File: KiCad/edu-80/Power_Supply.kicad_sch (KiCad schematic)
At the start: 19 parts, among them P1 Wall plug, Q21 2N3055, Q22 2N3906, SW1 SW_SPST, U22 uA7805

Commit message: Cleaning up the PAL-003 decoding, adding Modifications page.
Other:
- company: (none) -> Strangers
- title: (none) -> Edu-80 Z80 Trainer
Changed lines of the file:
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@@
 (kicad_sch (version 20230121) (generator eeschema)
   (paper "A")
+  (title_block
+    (title "Edu-80 Z80 Trainer")
+    (date "2023-06-03")
+    (rev "0.1")
+    (company "Strangers")
+    (comment 1 "Author: James D. Tucker")
+  )
   (junction (at 193.04 77.47) (diameter 0) (color 0 0 0 0)
   )

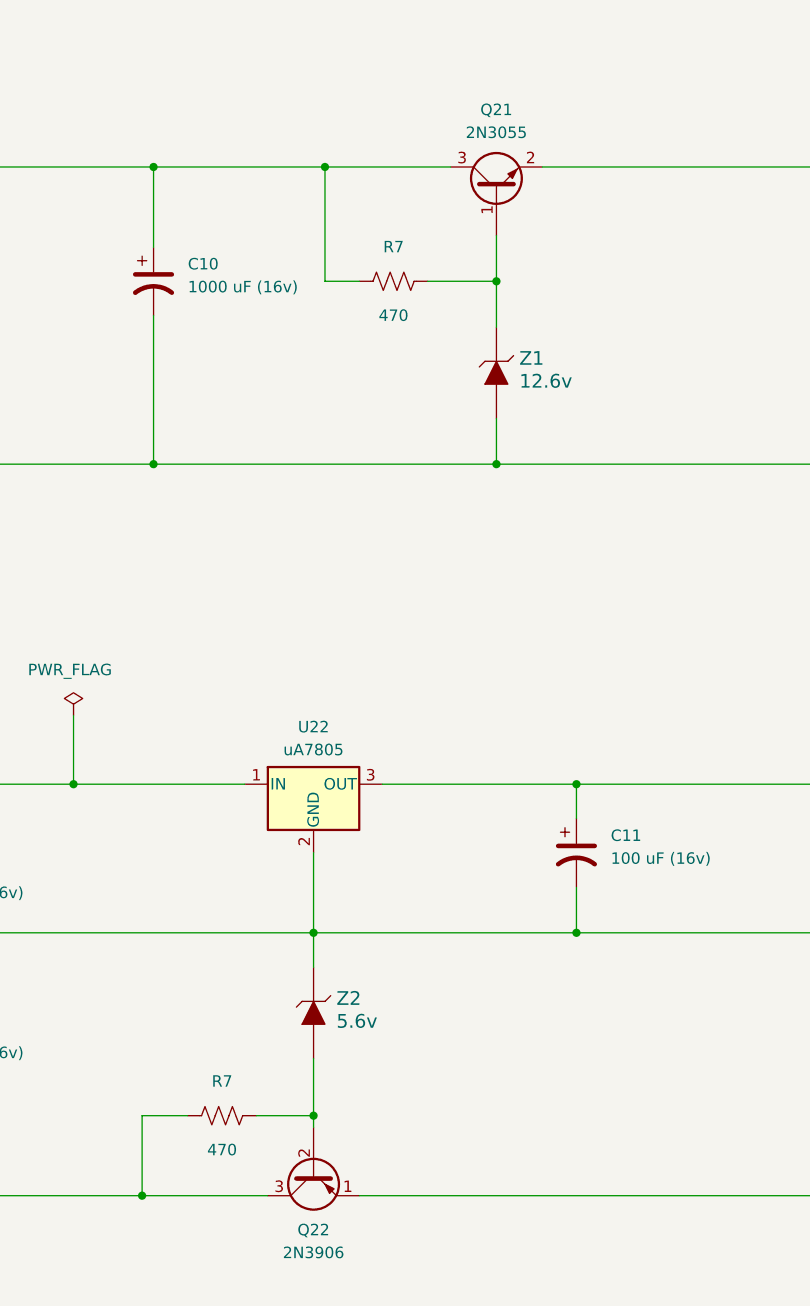
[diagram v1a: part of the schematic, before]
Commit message: Fixed ~IRQ vs. INT for PIO/CTC. Removed old (version 5) schematic files.
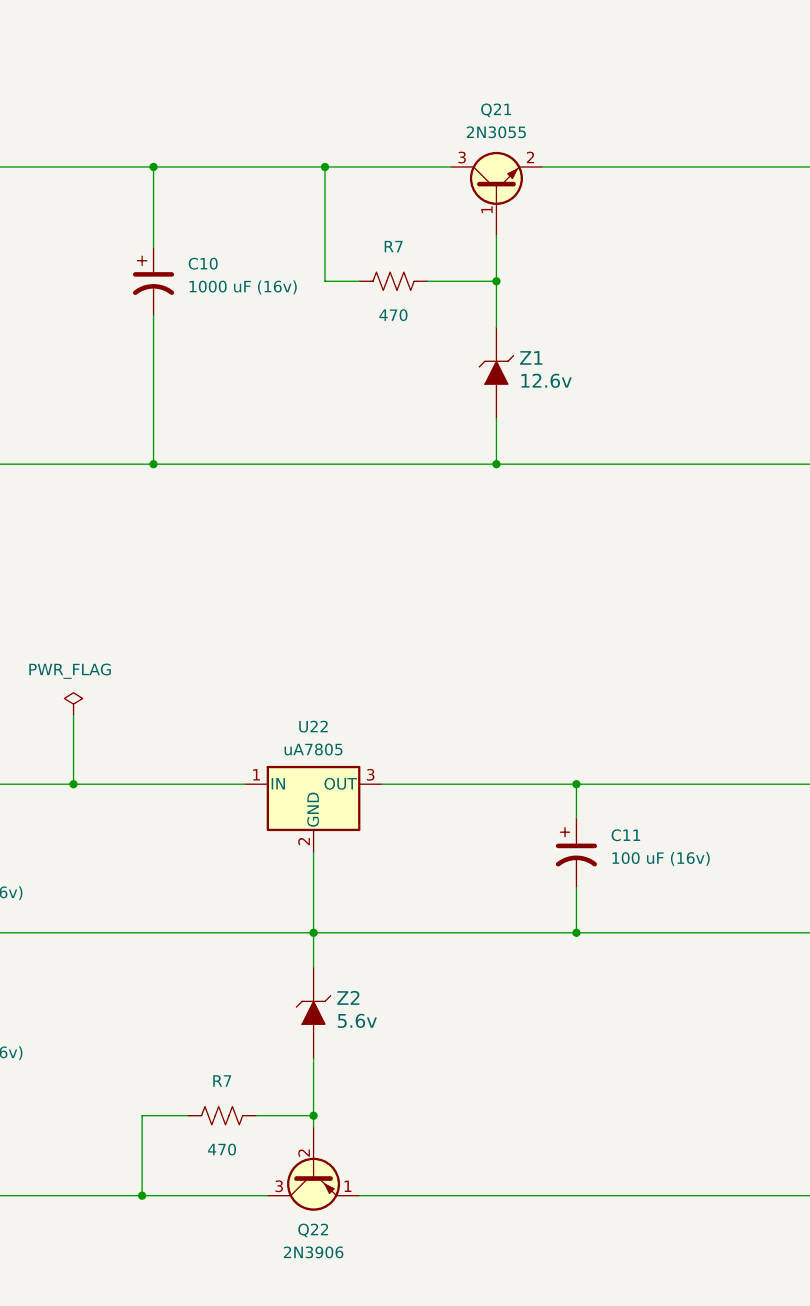
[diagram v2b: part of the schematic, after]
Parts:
- Q21: symbol Transistor_BJT:2N3055 -> Edu-80_Symbols:2N3055
- Q22: symbol Transistor_BJT:2N3906 -> Edu-80_Symbols:2N3905
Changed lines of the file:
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@@
   (title_block
     (title "Edu-80 Z80 Trainer")
-    (date "2023-06-03")
+    (date "2023-06-05")
     (rev "0.1")
     (company "Strangers")
-    (comment 1 "Author: James D. Tucker")
+    (comment 4 "Author: James D. Tucker")
   )
   (junction (at 193.04 77.47) (diameter 0) (color 0 0 0 0)
@@
     )
   )
-  (symbol (lib_id "Transistor_BJT:2N3906") (at 172.72 156.21 90) (mirror x) (unit 1)
+  (symbol (lib_id "Edu-80_Symbols:2N3905") (at 172.72 156.21 90) (mirror x) (unit 1)
     (in_bom yes) (on_board yes) (dnp no) (fields_autoplaced)
     (property "Reference" "Q22" (at 172.72 162.56 90)
@@
       (effects (font (size 1.27 1.27) italic) (justify left) hide)
     )
-    (property "Datasheet" "https://www.onsemi.com/pub/Collateral/2N3906-D.PDF" (at 172.72 156.21 0)
+    (property "Datasheet" "https://www.nteinc.com/specs/original/2N3905_06.pdf" (at 172.72 156.21 0)
       (effects (font (size 1.27 1.27)) (justify left) hide)
     )
@@
     )
   )
-  (symbol (lib_id "Transistor_BJT:2N3055") (at 193.04 46.99 90) (unit 1)
+  (symbol (lib_id "Edu-80_Symbols:2N3055") (at 193.04 46.99 90) (unit 1)
     (in_bom yes) (on_board yes) (dnp no) (fields_autoplaced)
     (property "Reference" "Q21" (at 193.04 38.1 90)

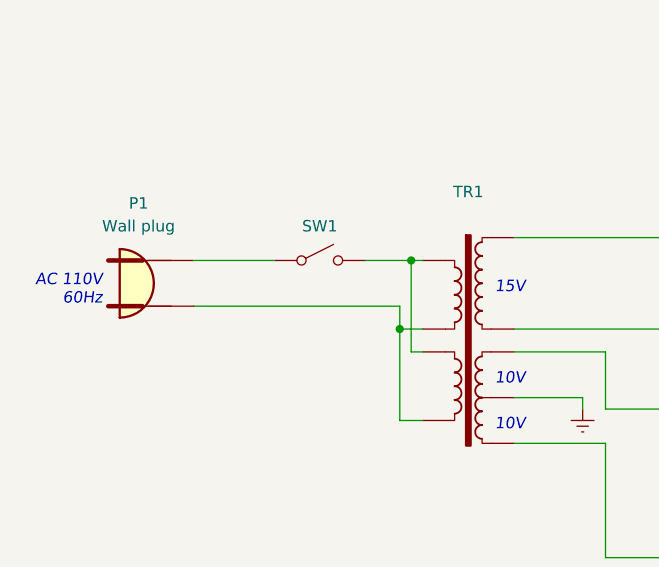
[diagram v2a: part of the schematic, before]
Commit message: Fixed the last of the EDR warnings/errors, adding footprints
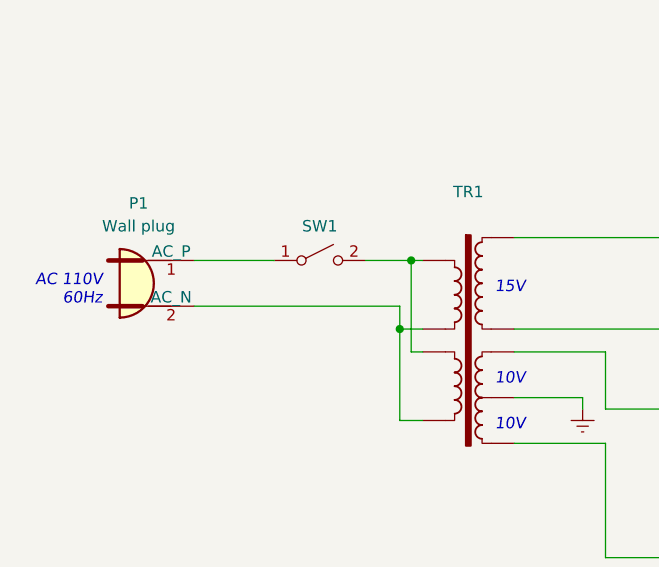
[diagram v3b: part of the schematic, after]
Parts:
- TR1: footprint (none) -> Transformer_THT:Transformer_Breve_TEZ-28x33
- Z1, Z2: footprint (none) -> digikey-footprints:SOD-123; Category (none) -> Discrete Semiconductor Products; Digi-Key_PN (none) -> MMSZ5231B-FDICT-ND; MPN (none) -> MMSZ5231B-7-F
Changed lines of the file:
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@@
       (effects (font (size 1.27 1.27)) hide)
     )
-    (property "Footprint" "" (at 63.5 116.84 0)
+    (property "Footprint" "Transformer_THT:Transformer_Breve_TEZ-28x33" (at 63.5 116.84 0)
       (effects (font (size 1.27 1.27)) hide)
     )
@@
       (effects (font (size 1.524 1.524)) (justify right))
     )
-    (property "Footprint" "" (at 187.96 62.23 0)
-      (effects (font (size 1.524 1.524)) (justify left) hide)
-    )
-    (property "Datasheet" "" (at 185.42 62.23 0)
-      (effects (font (size 1.524 1.524)) (justify left) hide)
-    )
-    (property "Digi-Key_PN" "" (at 182.88 62.23 0)
-      (effects (font (size 1.524 1.524)) (justify left) hide)
-    )
-    (property "MPN" "" (at 180.34 62.23 0)
-      (effects (font (size 1.524 1.524)) (justify left) hide)
-    )
-    (property "Category" "" (at 177.8 62.23 0)
+    (property "Footprint" "digikey-footprints:SOD-123" (at 187.96 62.23 0)
+      (effects (font (size 1.524 1.524)) (justify left) hide)
+    )
+    (property "Datasheet" "https://www.diodes.com/assets/Datasheets/ds18010.pdf" (at 185.42 62.23 0)
+      (effects (font (size 1.524 1.524)) (justify left) hide)
+    )
+    (property "Digi-Key_PN" "MMSZ5231B-FDICT-ND" (at 182.88 62.23 0)
+      (effects (font (size 1.524 1.524)) (justify left) hide)
+    )
+    (property "MPN" "MMSZ5231B-7-F" (at 180.34 62.23 0)
+      (effects (font (size 1.524 1.524)) (justify left) hide)
+    )
+    (property "Category" "Discrete Semiconductor Products" (at 177.8 62.23 0)
       (effects (font (size 1.524 1.524)) (justify left) hide)
     )
@@
       (effects (font (size 1.524 1.524)) (justify right))
     )
-    (property "Footprint" "" (at 167.64 133.35 0)
-      (effects (font (size 1.524 1.524)) (justify left) hide)
-    )
-    (property "Datasheet" "" (at 165.1 133.35 0)
-      (effects (font (size 1.524 1.524)) (justify left) hide)
-    )
-    (property "Digi-Key_PN" "" (at 162.56 133.35 0)
-      (effects (font (size 1.524 1.524)) (justify left) hide)
-    )
-    (property "MPN" "" (at 160.02 133.35 0)
-      (effects (font (size 1.524 1.524)) (justify left) hide)
-    )
-    (property "Category" "" (at 157.48 133.35 0)
-      (effects (font (size 1.524 1.524)) (justify left) hide)
-    )
+    (property "Footprint" "digikey-footprints:SOD-123" (at 167.64 133.35 0)
+      (effects (font (size 1.524 1.524)) (justify left) hide)
+    )
+    (property "Datasheet" "https://www.diodes.com/assets/Datasheets/ds18010.pdf" (at 165.1 133.35 0)
+      (effects (font (size 1.524 1.524)) (justify left) hide)
+    )
+    (property "Digi-Key_PN" "MMSZ5231B-FDICT-ND" (at 162.56 133.35 0)
+      (effects (font (size 1.524 1.524)) (justify left) hide)
+    )
+    (property "MPN" "MMSZ5231B-7-F" (at 160.02 133.35 0)
+      (effects (font (size 1.524 1.524)) (justify left) hide)
+    )
+    (property "Category" "Discrete Semiconductor Products" (at 157.48 133.35 0)
+      (effects (font (size 1.524 1.524)) (justify left) hide)
+    )

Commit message: Adding footprints.
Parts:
- C10, C11, C12, C13: footprint (none) -> Capacitor_THT:CP_Radial_D10.0mm_P2.50mm_P5.00mm
- D6: footprint (none) -> Diode_THT:Diode_Bridge_15.1x15.1x6.3mm_P10.9mm
- R7: footprint (none) -> Resistor_THT:R_Axial_DIN0309_L9.0mm_D3.2mm_P25.40mm_Horizontal
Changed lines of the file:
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@@
       (effects (font (size 1.27 1.27)))
     )
-    (property "Footprint" "" (at 181.356 58.166 90)
+    (property "Footprint" "Resistor_THT:R_Axial_DIN0309_L9.0mm_D3.2mm_P25.40mm_Horizontal" (at 181.356 58.166 90)
       (effects (font (size 1.27 1.27)) hide)
     )
@@
       (effects (font (size 1.27 1.27)))
     )
-    (property "Footprint" "" (at 162.306 150.876 90)
+    (property "Footprint" "Resistor_THT:R_Axial_DIN0309_L9.0mm_D3.2mm_P25.40mm_Horizontal" (at 162.306 150.876 90)
       (effects (font (size 1.27 1.27)) hide)
     )
@@
       (effects (font (size 1.27 1.27)) (justify left))
     )
-    (property "Footprint" "" (at 154.94 57.15 0)
+    (property "Footprint" "Capacitor_THT:CP_Radial_D10.0mm_P2.50mm_P5.00mm" (at 154.94 57.15 0)
       (effects (font (size 1.27 1.27)) hide)
     )
@@
       (effects (font (size 1.27 1.27)) hide)
     )
-    (property "Footprint" "" (at 102.87 67.31 0)
+    (property "Footprint" "Diode_THT:Diode_Bridge_15.1x15.1x6.3mm_P10.9mm" (at 102.87 67.31 0)
       (effects (font (size 1.27 1.27)) hide)
     )
@@
       (effects (font (size 1.27 1.27)) (justify left))
     )
-    (property "Footprint" "" (at 124.46 124.46 0)
+    (property "Footprint" "Capacitor_THT:CP_Radial_D10.0mm_P2.50mm_P5.00mm" (at 124.46 124.46 0)
       (effects (font (size 1.27 1.27)) hide)
     )
@@
       (effects (font (size 1.27 1.27)) (justify left))
     )
-    (property "Footprint" "" (at 201.93 120.65 0)
+    (property "Footprint" "Capacitor_THT:CP_Radial_D10.0mm_P2.50mm_P5.00mm" (at 201.93 120.65 0)
       (effects (font (size 1.27 1.27)) hide)
     )
@@
       (effects (font (size 1.27 1.27)) (justify left))
     )
-    (property "Footprint" "" (at 124.46 142.24 0)
-      (effects (font (size 1.27 1.27)) hide)
-    )
+    (property "Footprint" "Capacitor_THT:CP_Radial_D10.0mm_P2.50mm_P5.00mm" (at 124.46 142.24 0)
+      (effects (font (size 1.27 1.27)) hide)
+    )
